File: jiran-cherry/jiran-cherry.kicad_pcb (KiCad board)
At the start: 2 copper layers, 152.3 x 104.7 mm, 74 parts, among them J1 TRRS, SW1 SW_Push, SW10 SW_Push, SW11 SW_Push, SW12 SW_Push, SW13 SW_Push, SW14 SW_Push, SW15 SW_Push, SW16 SW_Push, SW17 SW_Push, SW18 SW_Push, SW19 SW_Push, SW2 SW_Push, SW20 SW_Push, SW21 SW_Push, SW22 SW_Push, SW23 SW_Push, SW24 SW_Push, SW25 SW_Push, SW26 SW_Push, SW27 SW_Push, SW28 SW_Push, SW29 SW_Push, SW3 SW_Push, SW4 SW_Push, SW5 SW_Push, SW6 SW_Push, SW7 SW_Push, SW8 SW_Push, SW9 SW_Push, U1 ProMicro

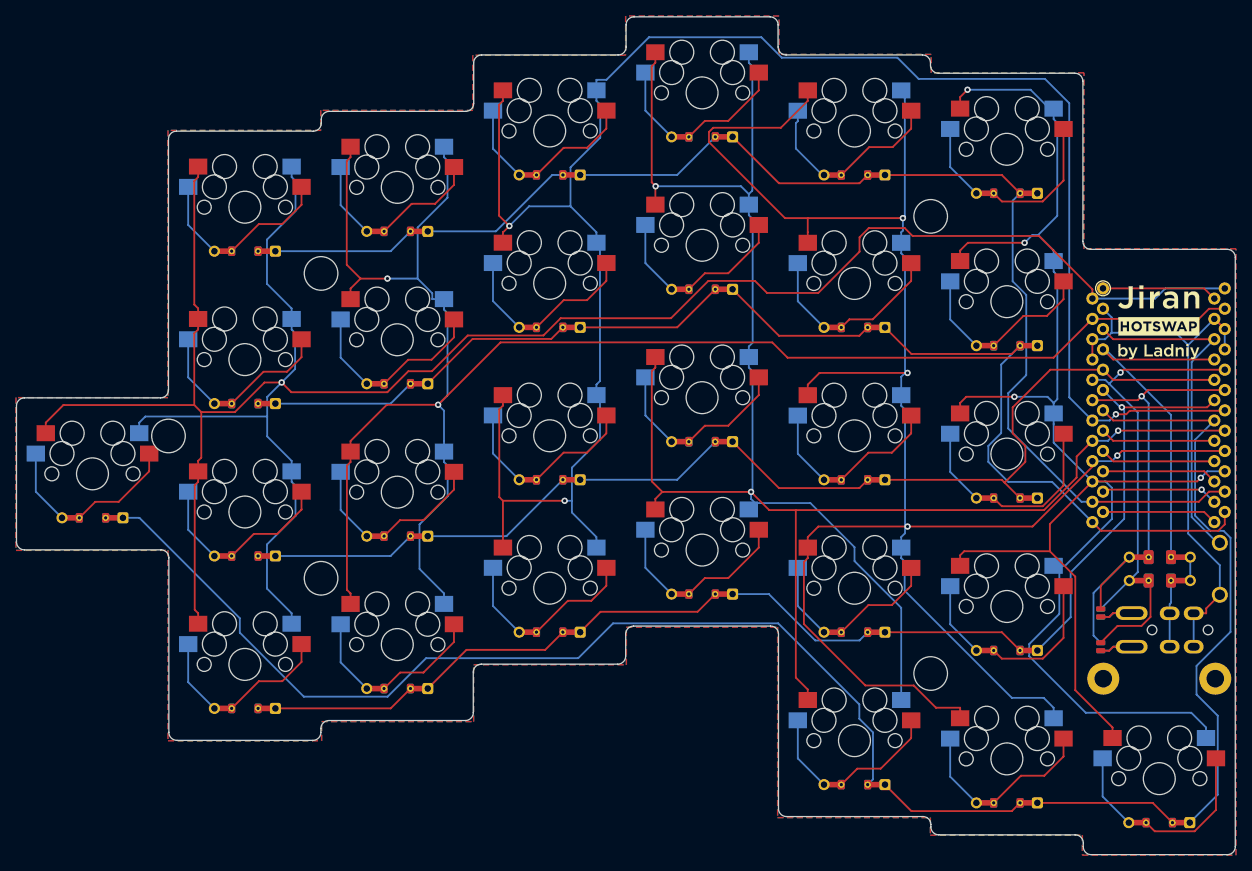
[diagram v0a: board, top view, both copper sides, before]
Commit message: Delete all tracks
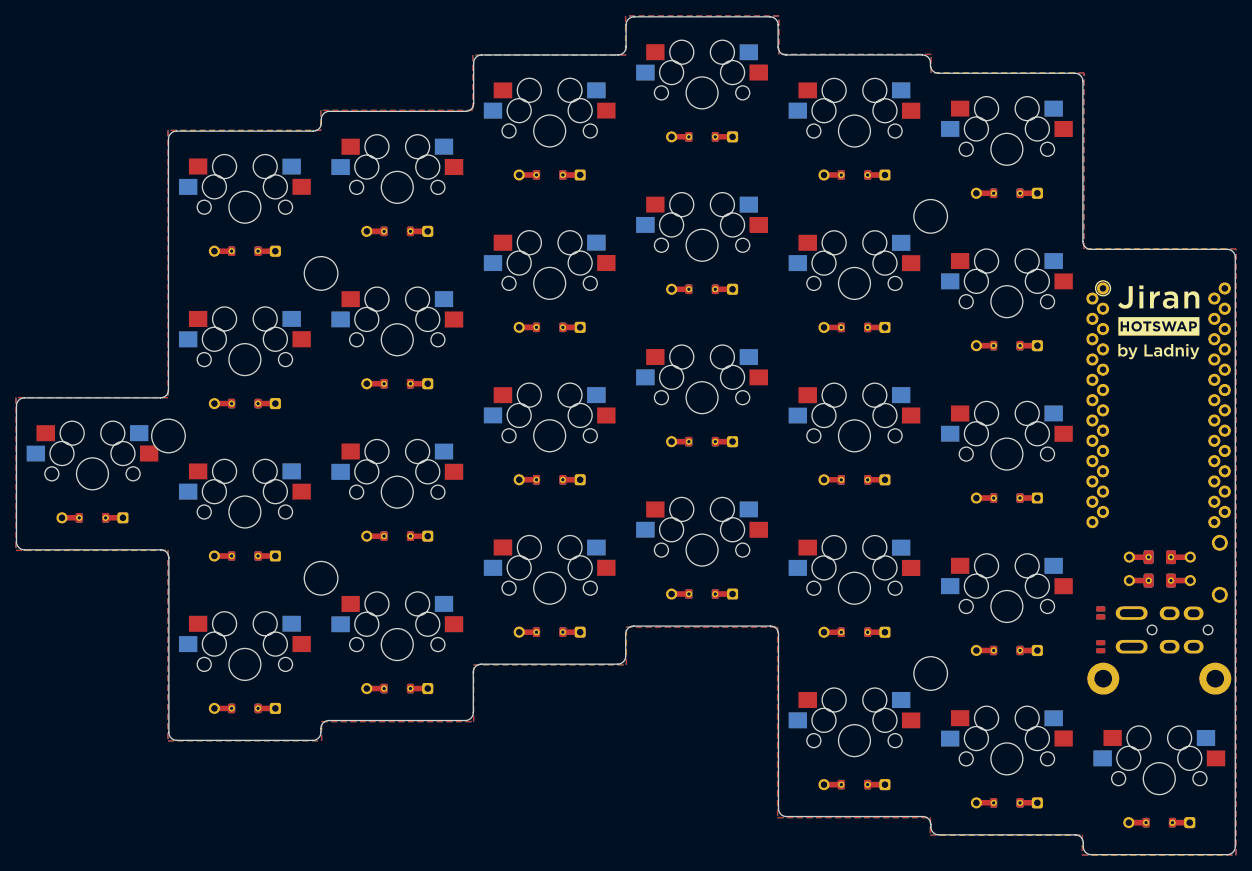
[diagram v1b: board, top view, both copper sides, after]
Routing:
- net /col0: track 308.6 -> 0.00 mm, vias 1 -> 0
- net /col3: track 247.8 -> 0.00 mm, vias 3 -> 0
- net /col4: track 245.9 -> 0.00 mm, vias 4 -> 0
- net /col2: track 245.2 -> 0.00 mm, vias 3 -> 0
- net /rowE: track 239.4 -> 0.00 mm
- net /col1: track 231.1 -> 0.00 mm, vias 2 -> 0
- net /col5: track 214.9 -> 0.00 mm, vias 4 -> 0
- net /rowA: track 169.9 -> 0.00 mm
- net /rowB: track 159.1 -> 0.00 mm
- net /rowD: track 157.3 -> 0.00 mm, vias 1 -> 0
- net /rowC: track 145.9 -> 0.00 mm
- net GND: track 69.5 -> 0.00 mm
- net SDA: track 63.7 -> 0.00 mm, vias 1 -> 0
- net SCL: track 60.8 -> 0.00 mm, vias 1 -> 0
- net VCC: track 60.2 -> 0.00 mm
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
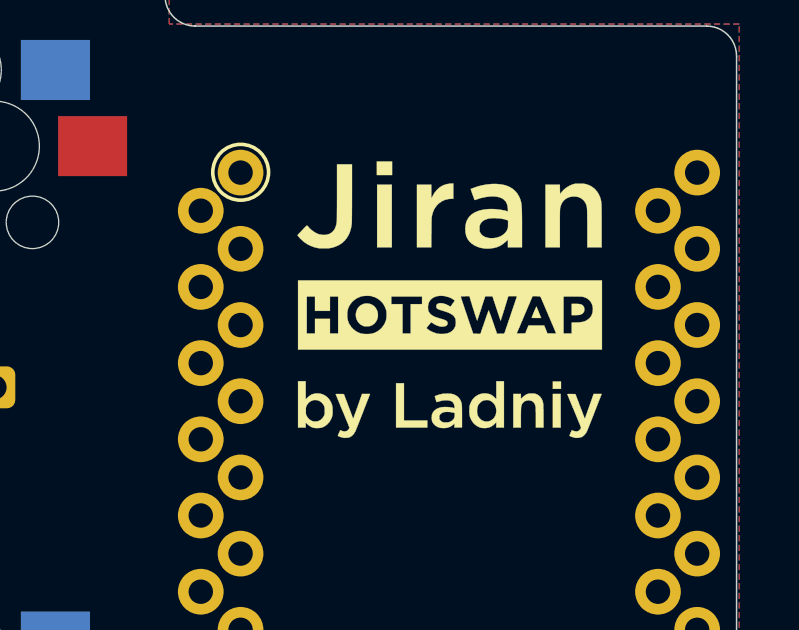
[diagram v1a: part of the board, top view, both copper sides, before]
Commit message: Update logos on pcb
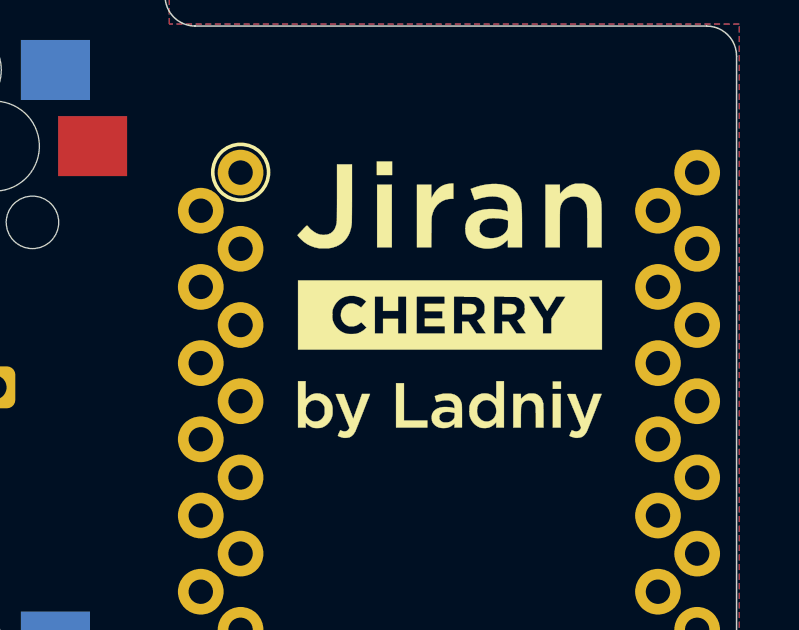
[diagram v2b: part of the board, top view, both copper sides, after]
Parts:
- G1, G2: footprint used_footprints:Silk_Logo_Hotswap -> used_footprints:Silk_Logo_Cherry

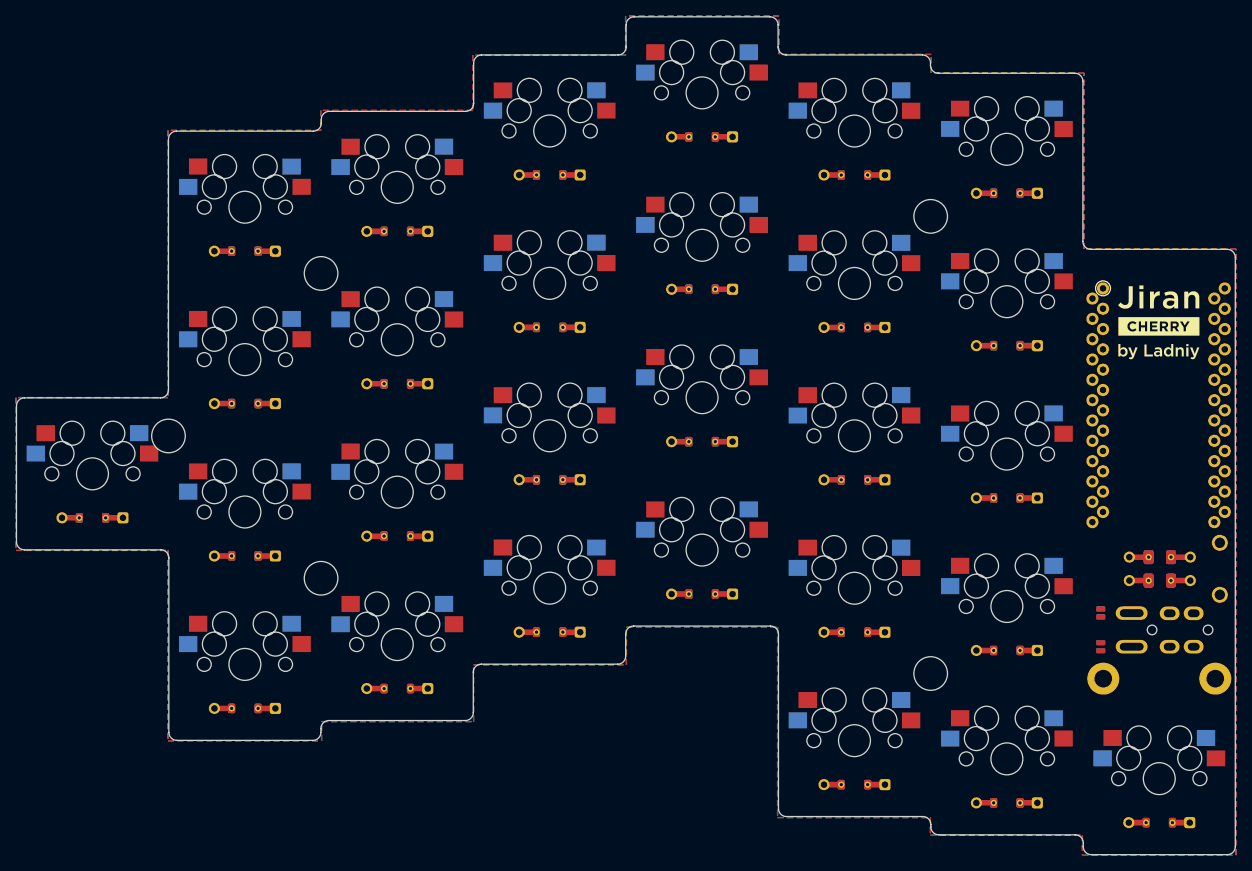
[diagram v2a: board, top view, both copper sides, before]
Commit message: Change switch footprints
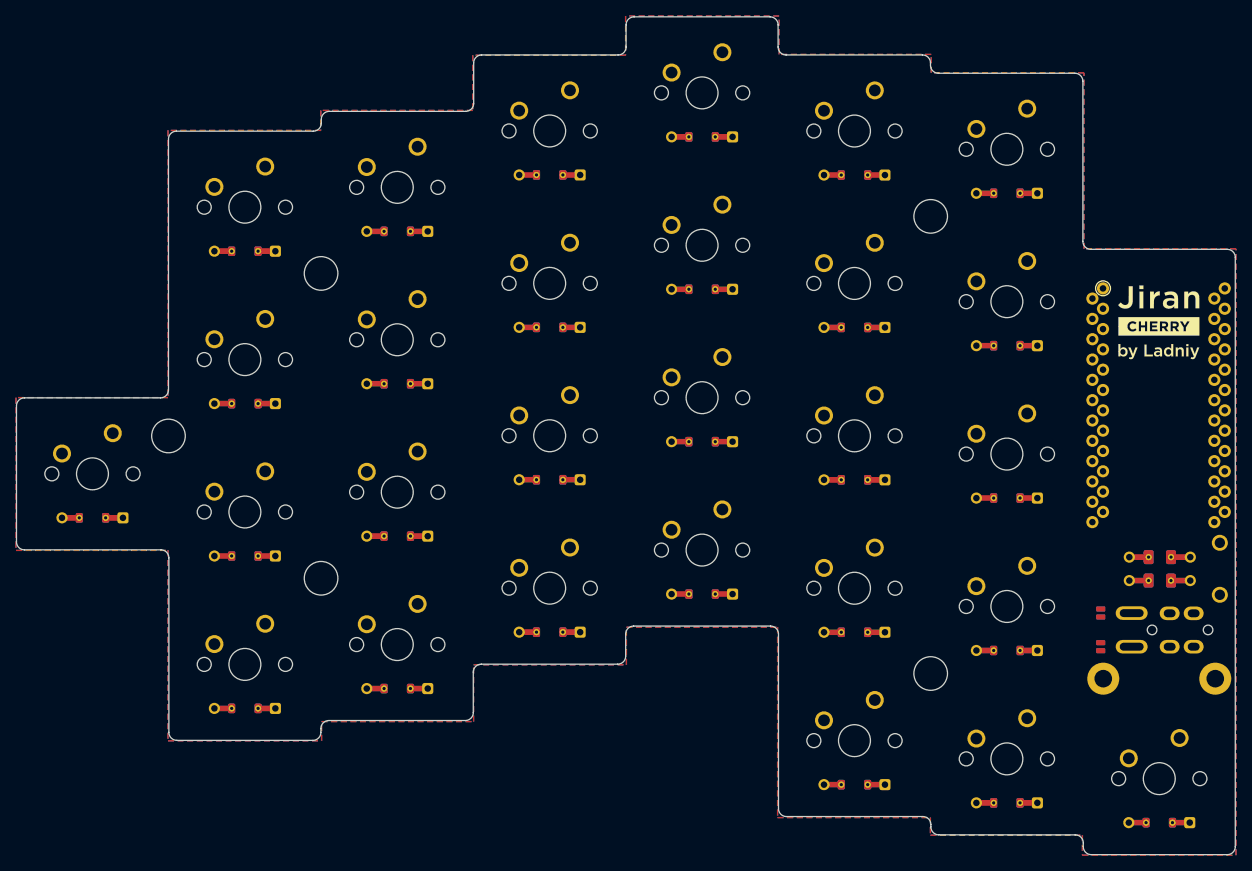
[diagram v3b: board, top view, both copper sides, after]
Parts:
- SW1, SW10, SW11, SW12, SW13, SW14, SW15, SW16, SW17, SW18, SW19, SW2, SW20, SW21, SW22, SW23, SW24, SW25, SW26, SW27, SW28, SW3, SW4, SW5, SW6, SW7, SW8, SW9: footprint used_footprints:Switch_Mx_Hotswap_1u -> used_footprints:Switch_Mx_Cherry_1u
